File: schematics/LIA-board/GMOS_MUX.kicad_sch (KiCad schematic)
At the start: 2 parts, among them IC1 TMUX6136, J1 DIP40_J19

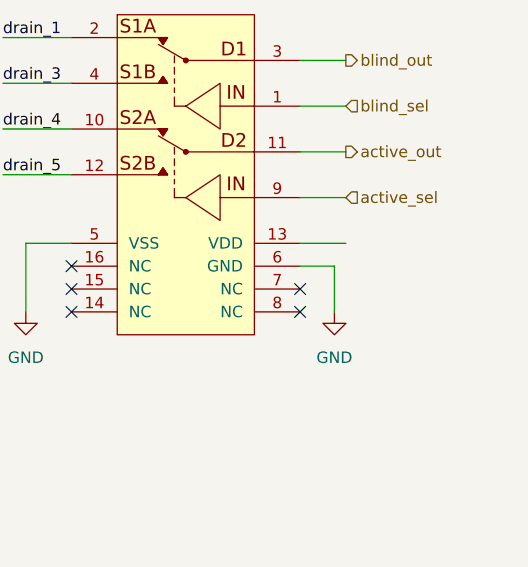
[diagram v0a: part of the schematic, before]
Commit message: added MCU
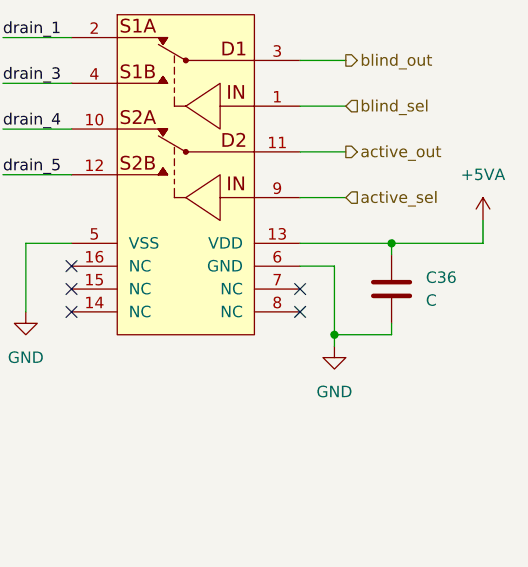
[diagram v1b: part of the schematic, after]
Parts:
- added C36: C, symbol Device:C
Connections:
- net +5VA: now also IC1.13 (VDD), C36.2
- net GND: now also C36.1
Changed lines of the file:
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@@
+	)
+	(junction
+		(at 226.06 83.82)
+		(diameter 0)
+		(color 0 0 0 0)
 	)
 	(junction
@@
 	)
 	(junction
+		(at 219.71 93.98)
+		(diameter 0)
+		(color 0 0 0 0)
+	)
+	(junction
 		(at 97.79 48.26)
 		(diameter 0)
@@
 	(wire
 		(pts
+			(xy 226.06 83.82) (xy 226.06 85.09)
+		)
+		(stroke
+			(width 0)
+			(type default)
+		)
+	)
+	(wire
+		(pts
 			(xy 64.77 90.17) (xy 80.01 90.17)
 		)
@@
 	(wire
 		(pts
+			(xy 236.22 81.28) (xy 236.22 83.82)
+		)
+		(stroke
+			(width 0)
+			(type default)
+		)
+	)
+	(wire
+		(pts
 			(xy 185.42 83.82) (xy 185.42 91.44)
 		)
@@
 	(wire
 		(pts
+			(xy 226.06 93.98) (xy 226.06 92.71)
+		)
+		(stroke
+			(width 0)
+			(type default)
+		)
+	)
+	(wire
+		(pts
 			(xy 80.01 64.77) (xy 76.2 64.77)
 		)
@@
 	(wire
 		(pts
+			(xy 226.06 83.82) (xy 236.22 83.82)
+		)
+		(stroke
+			(width 0)
+			(type default)
+		)
+	)
+	(wire
+		(pts
 			(xy 215.9 78.74) (xy 220.98 78.74)
 		)
@@
 	(wire
 		(pts
-			(xy 215.9 83.82) (xy 220.98 83.82)
+			(xy 215.9 83.82) (xy 226.06 83.82)
 		)
 		(stroke
@@
 	(wire
 		(pts
+			(xy 219.71 93.98) (xy 226.06 93.98)
+		)
+		(stroke
+			(width 0)
+			(type default)
+		)
+	)
+	(wire
+		(pts
 			(xy 73.66 59.69) (xy 73.66 67.31)
 		)
@@
 	(wire
 		(pts
+			(xy 219.71 93.98) (xy 219.71 95.25)
+		)
+		(stroke
+			(width 0)
+			(type default)
+		)
+	)
+	(wire
+		(pts
 			(xy 182.88 66.04) (xy 190.5 66.04)
 		)
@@
 	(wire
 		(pts
-			(xy 219.71 86.36) (xy 219.71 91.44)
+			(xy 219.71 86.36) (xy 219.71 93.98)
 		)
 		(stroke
@@
 	)
 	(symbol
+		(lib_id "power:+5VA")
+		(at 236.22 81.28 0)
+		(unit 1)
+		(body_style 1)
+		(exclude_from_sim no)
+		(in_bom yes)
+		(on_board yes)
+		(in_pos_files yes)
+		(dnp no)
+		(fields_autoplaced yes)
+		(property "Reference" "#PWR069"
+			(at 236.22 85.09 0)
+			(hide yes)
+			(show_name no)
+			(do_not_autoplace no)
+			(effects
+				(font
+					(size 1.27 1.27)
+				)
+			)
+		)
+		(property "Value" "+5VA"
+			(at 236.22 76.2 0)
+			(show_name no)
+			(do_not_autoplace no)
+			(effects
+				(font
+					(size 1.27 1.27)
+				)
+			)
+		)
+		(property "Footprint" ""
+			(at 236.22 81.28 0)
+			(hide yes)
+			(show_name no)
+			(do_not_autoplace no)
+			(effects
+				(font
+					(size 1.27 1.27)
+				)
+			)
+		)
+		(property "Datasheet" ""
+			(at 236.22 81.28 0)
+			(hide yes)
+			(show_name no)
+			(do_not_autoplace no)
+			(effects
+				(font
+					(size 1.27 1.27)
+				)
+			)
+		)
+		(property "Description" "Power symbol creates a global label with name \"+5VA\""
+			(at 236.22 81.28 0)
+			(hide yes)
+			(show_name no)
+			(do_not_autoplace no)
+			(effects
+				(font
+					(size 1.27 1.27)
+				)
+			)
+		)
+		(pin "1"
+		)
+		(instances
+			(project "GMOS-LIA"
+				(path "/87b3d1ed-39bd-4cff-a405-e580c48ff0ef/24d58a37-277c-4dbe-a5fe-38b4ef83cb3e"
+					(reference "#PWR069")
+					(unit 1)
+				)
+			)
+		)
+	)
+	(symbol
+		(lib_id "Device:C")
+		(at 226.06 88.9 180)
+		(unit 1)
+		(body_style 1)
+		(exclude_from_sim no)
+		(in_bom yes)
+		(on_board yes)
+		(in_pos_files yes)
+		(dnp no)
+		(fields_autoplaced yes)
+		(property "Reference" "C36"
+			(at 229.87 87.6299 0)
+			(show_name no)
+			(do_not_autoplace no)
+			(effects
+				(font
+					(size 1.27 1.27)
+				)
+				(justify right)
+			)
+		)
+		(property "Value" "C"
+			(at 229.87 90.1699 0)
+			(show_name no)
+			(do_not_autoplace no)
+			(effects
+				(font
+					(size 1.27 1.27)
+				)
+				(justify right)
+			)
+		)
+		(property "Footprint" ""
+			(at 225.0948 85.09 0)
+			(hide yes)
+			(show_name no)
+			(do_not_autoplace no)
+			(effects
+				(font
+					(size 1.27 1.27)
+				)
+			)
+		)
+		(property "Datasheet" ""
+			(at 226.06 88.9 0)
+			(hide yes)
+			(show_name no)
+			(do_not_autoplace no)
+			(effects
+				(font
+					(size 1.27 1.27)
+				)
+			)
+		)
+		(property "Description" "Unpolarized capacitor"
+			(at 226.06 88.9 0)
+			(hide yes)
+			(show_name no)
+			(do_not_autoplace no)
+			(effects
+				(font
+					(size 1.27 1.27)
+				)
+			)
+		)
+		(pin "1"
+		)
+		(pin "2"
+		)
+		(instances
+			(project "GMOS-LIA"
+				(path "/87b3d1ed-39bd-4cff-a405-e580c48ff0ef/24d58a37-277c-4dbe-a5fe-38b4ef83cb3e"
+					(reference "C36")
+					(unit 1)
+				)
+			)
+		)
+	)
+	(symbol
 		(lib_id "power:GND")
-		(at 219.71 91.44 0)
+		(at 219.71 95.25 0)
 		(unit 1)
 		(body_style 1)
@@
 		(fields_autoplaced yes)
 		(property "Reference" "#PWR042"
-			(at 219.71 97.79 0)
+			(at 219.71 101.6 0)
 			(hide yes)
 			(show_name no)
@@
 		)
 		(property "Value" "GND"
-			(at 219.71 96.52 0)
+			(at 219.71 100.33 0)
 			(show_name no)
 			(do_not_autoplace no)
@@
 		)
 		(property "Footprint" ""
-			(at 219.71 91.44 0)
+			(at 219.71 95.25 0)
 			(hide yes)
 			(show_name no)
@@
 		)
 		(property "Datasheet" ""
-			(at 219.71 91.44 0)
+			(at 219.71 95.25 0)
 			(hide yes)
 			(show_name no)
@@
 		)
 		(property "Description" "Power symbol creates a global label with name \"GND\" , ground"
-			(at 219.71 91.44 0)
-			(hide yes)
-			(show_name no)
+			(at 219.71 95.25 0)
+			(hide yes)
+			(show_name no)

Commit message: slight modifications to scenamtic
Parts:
- added C37, C38, C39, C40: C, symbol Device:C
- added R35, R36, R37, R38, R39, R40, R41, R42: 50k, SparkFun-Resistor:R_0603_1608Metric, symbol SparkFun:R
- added U16, U17: OPA2196xD, Package_SO:SOIC-8_3.9x4.9mm_P1.27mm, symbol Amplifier_Operational:OPA2196xD
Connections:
- net +5VA: now also C37.2, C39.2, U16.8 (V+), U17.8 (V+)
- net GND: now also C37.1, C38.2, C39.1, C40.2
- new net: R40.1, R42.2, U17.6 (-)
- new net: R42.1, U17.7
- new net: R35.1, R36.2, U16.2 (-)
- new net: R37.2, R38.1, U16.6 (-)
- new net: R37.1, U16.7
- new net: R36.1, U16.1
- new net: R41.1, U17.1
- new net: R39.1, R41.2, U17.2 (-)
- new net -5VA: C38.1, C40.1, U16.4 (V-), U17.4 (V-)
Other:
- moved on the sheet: C36, IC1, J1

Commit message: modified scematic
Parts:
- removed C37, C38, C39, C40: C, symbol Device:C
- removed R35, R36, R37, R38, R39, R40, R41, R42: 50k, SparkFun-Resistor:R_0603_1608Metric, symbol SparkFun:R
- removed U16, U17: OPA2196xD, Package_SO:SOIC-8_3.9x4.9mm_P1.27mm, symbol Amplifier_Operational:OPA2196xD
- added C41, C42: C, symbol Device:C
- added IC6, IC7: TMUX6136, symbol CERN:TMUX6136PW_a
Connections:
- net +5VA: now also C41.2, C42.2, IC6.13 (VDD), IC7.13 (VDD)
- net GND: now also C41.1, C42.1, IC6.5 (VSS), IC6.6 (GND), IC7.5 (VSS), IC7.6 (GND)
- net active_sel: now also IC6.9 (SEL2), IC7.9 (SEL2)
- net blind_sel: now also IC6.1 (SEL1), IC7.1 (SEL1)
- net drain_1: now also IC6.2 (S1A)
- net drain_3: now also IC6.4 (S1B)
- net drain_4: now also IC6.10 (S2A)
- net drain_5: now also IC6.12 (S2B)
- net heater_1: now also IC7.2 (S1A)
- net heater_3: now also IC7.4 (S1B)
- net heater_4: now also IC7.10 (S2A)
- net heater_5: now also IC7.12 (S2B)
- new net active_drain_voltage: IC6.11 (D2)
- new net active_heater_voltage: IC7.11 (D2)
- new net blind_drain_voltage: IC6.3 (D1)
- new net blind_heater_voltage: IC7.3 (D1)
- no-connect marks 5 -> 15
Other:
- moved on the sheet: J1

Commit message: modified some of the scenatics
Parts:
- added R47, R48, R49, R50: 330k, SparkFun-Resistor:R_0603_1608Metric, symbol SparkFun:R
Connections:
- net drain_1: now also R47.1; no longer IC6.2 (S1A)
- net drain_3: now also R48.1; no longer IC6.4 (S1B)
- net drain_4: now also R49.1; no longer IC6.10 (S2A)
- net drain_5: now also R50.1; no longer IC6.12 (S2B)
- new net: IC6.12 (S2B), R50.2
- new net: IC6.10 (S2A), R49.2
- new net: IC6.2 (S1A), R47.2
- new net: IC6.4 (S1B), R48.2

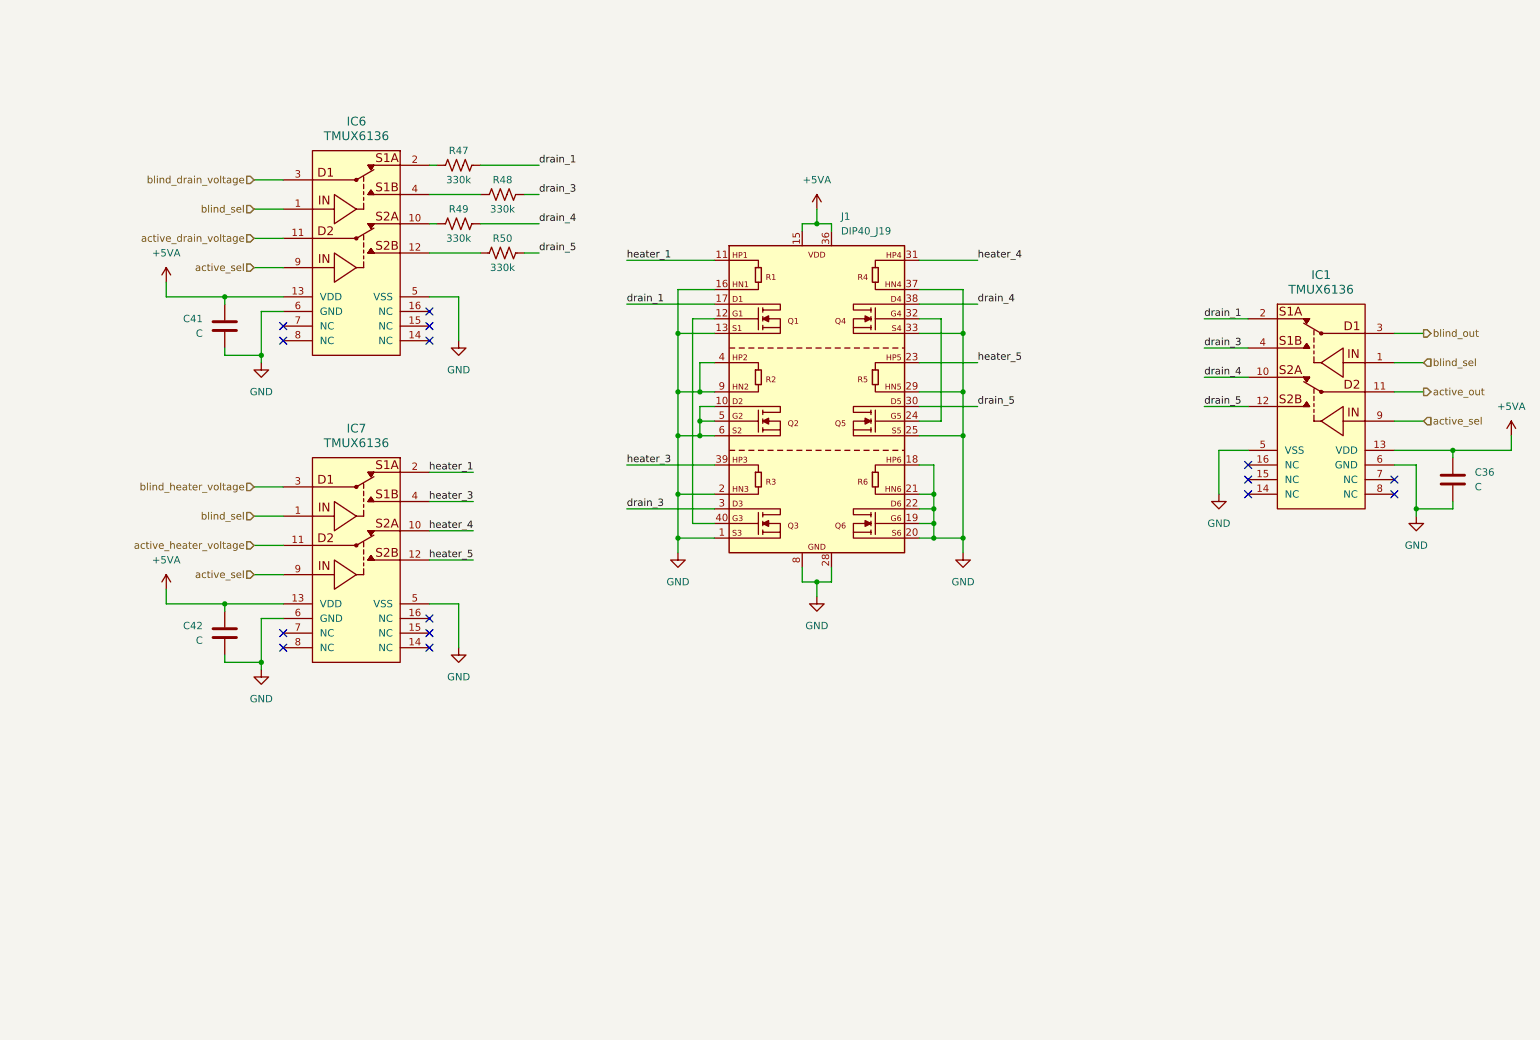
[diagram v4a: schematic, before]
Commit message: commit before changing the oscillator implementation
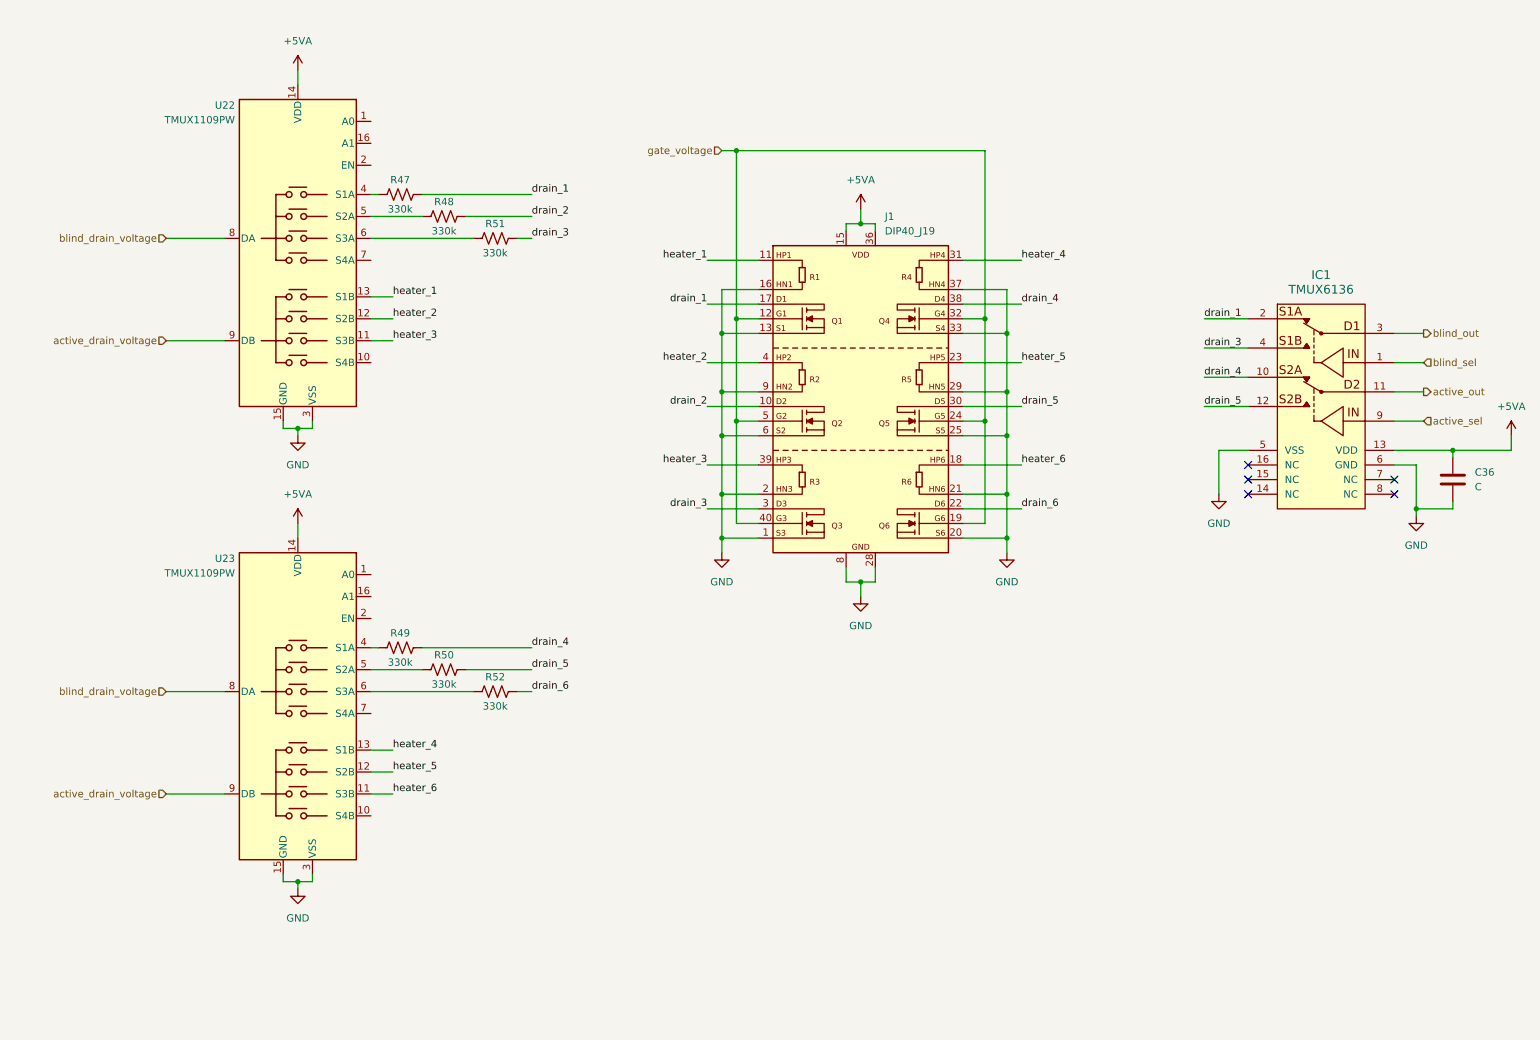
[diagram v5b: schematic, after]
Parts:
- removed C41, C42: C, symbol Device:C
- removed IC6, IC7: TMUX6136, symbol CERN:TMUX6136PW_a
- added R51, R52: 330k, SparkFun-Resistor:R_0603_1608Metric, symbol SparkFun:R
- added U22, U23: TMUX1109PW, Package_SO:TSSOP-16_4.4x5mm_P0.65mm, symbol device_libraries:TMUX1109PW
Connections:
- net +5VA: now also U22.14 (VDD), U23.14 (VDD)
- net GND: now also U22.15 (GND), U22.3 (VSS), U23.15 (GND), U23.3 (VSS); no longer J1.10 (D2), J1.18 (HP6), J1.19 (G6), J1.22 (D6), J1.4 (HP2), J1.5 (G2)
- net active_drain_voltage: now also U22.9 (DB), U23.9 (DB)
- net blind_drain_voltage: now also U22.8 (DA), U23.8 (DA)
- net drain_3: now also R51.1; no longer R48.1
- net heater_1: now also U22.13 (S1B)
- net heater_3: now also U22.11 (S3B)
- net heater_4: now also U23.13 (S1B)
- net heater_5: now also U23.12 (S2B)
- net at R50.2: now also U23.5 (S2A)
- net gate_voltage: now reaches J1.12 (G1), J1.40 (G3)
- net gate_voltage: now also J1.19 (G6), J1.24 (G5), J1.32 (G4), J1.5 (G2)
- net at R49.2: now also U23.4 (S1A)
- net at R47.2: now also U22.4 (S1A)
- net at R48.2: now also U22.5 (S2A)
- new net: R52.2, U23.6 (S3A)
- new net: R51.2, U22.6 (S3A)
- new net drain_2: J1.10 (D2), R48.1
- new net drain_6: J1.22 (D6), R52.1
- new net heater_2: J1.4 (HP2), U22.12 (S2B)
- new net heater_6: J1.18 (HP6), U23.11 (S3B)
- no-connect marks 15 -> 5
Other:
- moved on the sheet: J1

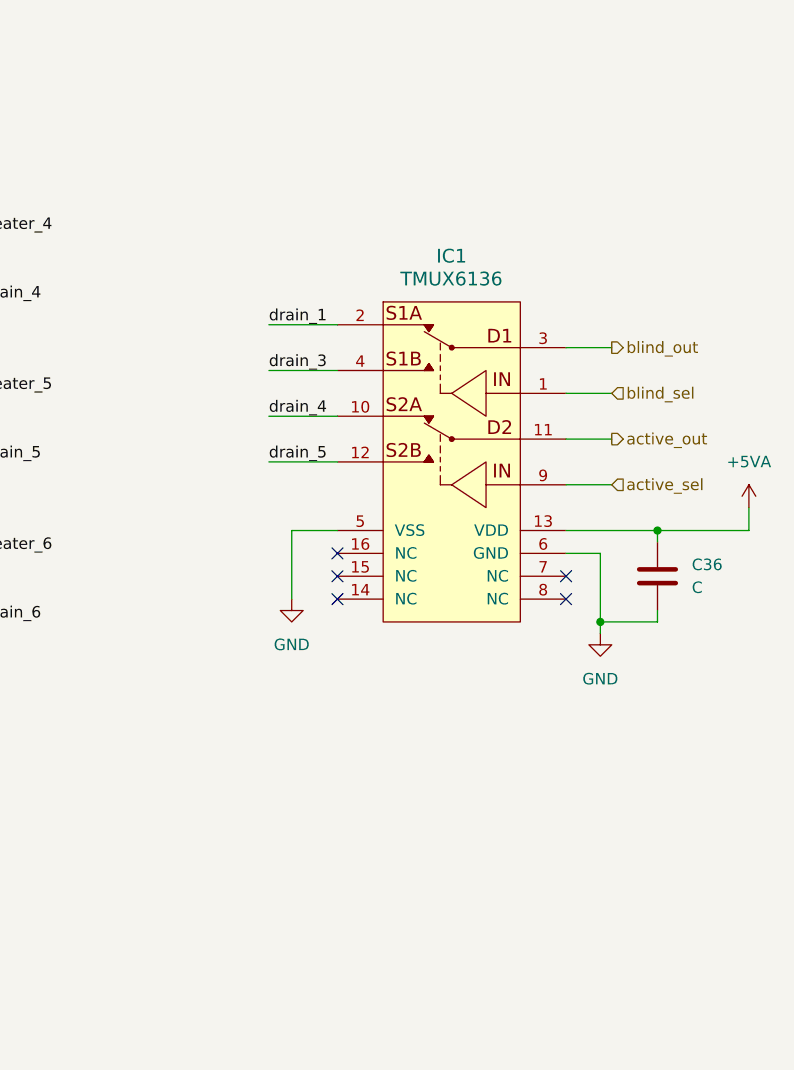
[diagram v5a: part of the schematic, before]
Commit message: new oscillator, not tested in simulation yet
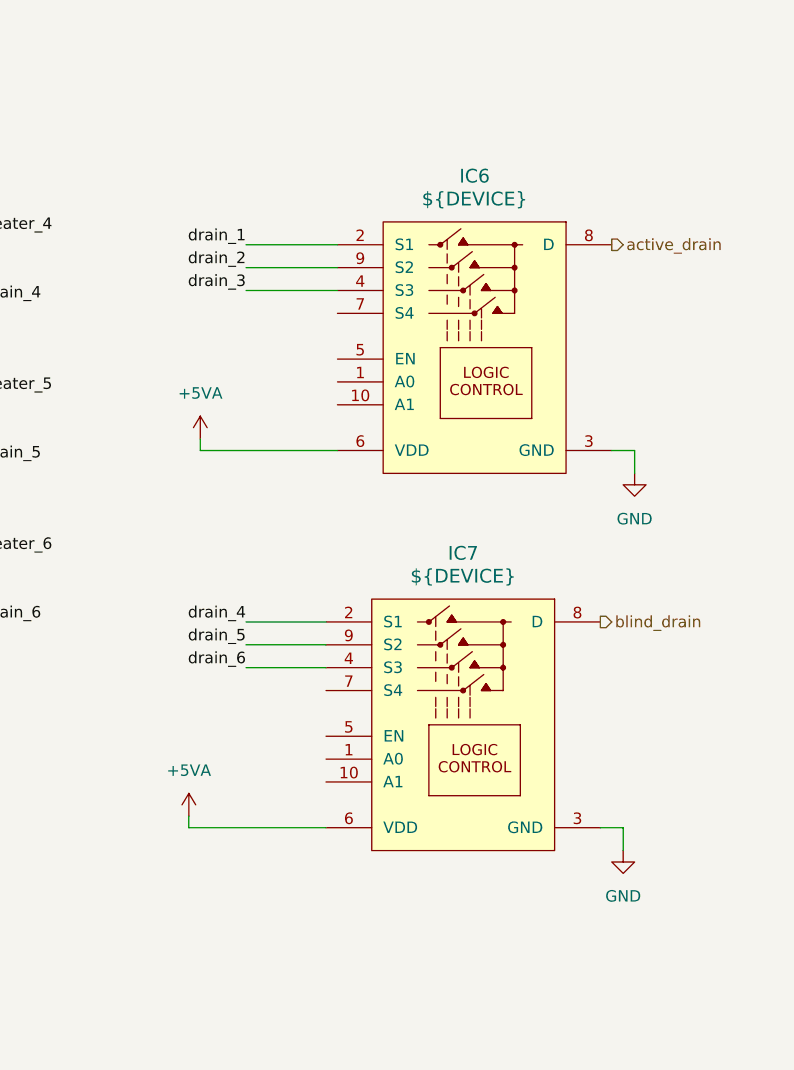
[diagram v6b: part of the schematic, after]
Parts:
- removed C36: C, symbol Device:C
- removed IC1: TMUX6136, symbol CERN:TMUX6136PW_a
- added IC6, IC7: ${DEVICE}, symbol CERN:TMUX1104
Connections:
- net +5VA: now also IC6.6 (VDD), IC7.6 (VDD)
- net GND: now also IC6.3 (GND), IC7.3 (GND)
- net drain_1: now also IC6.2 (S1)
- net drain_2: now also IC6.9 (S2)
- net drain_3: now also IC6.4 (S3)
- net drain_4: now also IC7.2 (S1)
- net drain_5: now also IC7.9 (S2)
- net drain_6: now also IC7.4 (S3)
- new net active_drain: IC6.8 (D)
- new net blind_drain: IC7.8 (D)
- no-connect marks 5 -> 0

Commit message: commit before changing LIA
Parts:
- removed IC6, IC7: ${DEVICE}, symbol CERN:TMUX1104
- removed J1: DIP40_J19, Package_DIP:DIP-40_W15.24mm, symbol device_libraries:DIP40_J19
- removed R47, R48, R49, R50, R51, R52: 330k, SparkFun-Resistor:R_0603_1608Metric, symbol SparkFun:R
- removed U22, U23: TMUX1109PW, Package_SO:TSSOP-16_4.4x5mm_P0.65mm, symbol device_libraries:TMUX1109PW
